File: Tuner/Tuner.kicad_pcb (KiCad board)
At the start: 2 copper layers, 74 parts, among them J1 Barrel_Jack, J2 Input, J3 Conn_01x04_Pin, J4 SWD, J5 output channel, J6 TIM1 output, Q1 NPN, Q2 NPN, Q3 NPN, Q4 NPN, Q5 NPN, SW1 NRST, SW2 SW_SPDT, U1 NE5532, U2 AMS1117-3.3, U3 STM32F411RETx, Y1 16Mhz

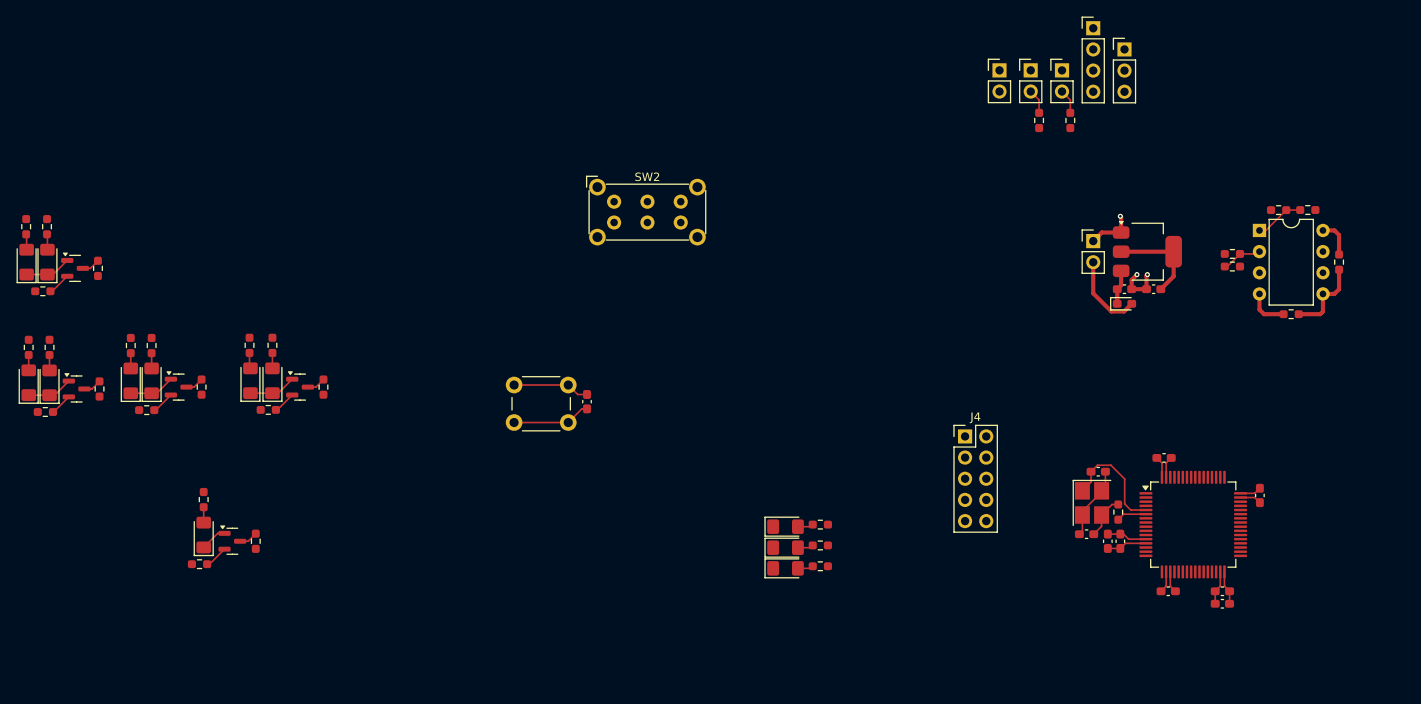
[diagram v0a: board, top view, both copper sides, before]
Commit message: removed the LED drivers and finished first layout placement for the PCB
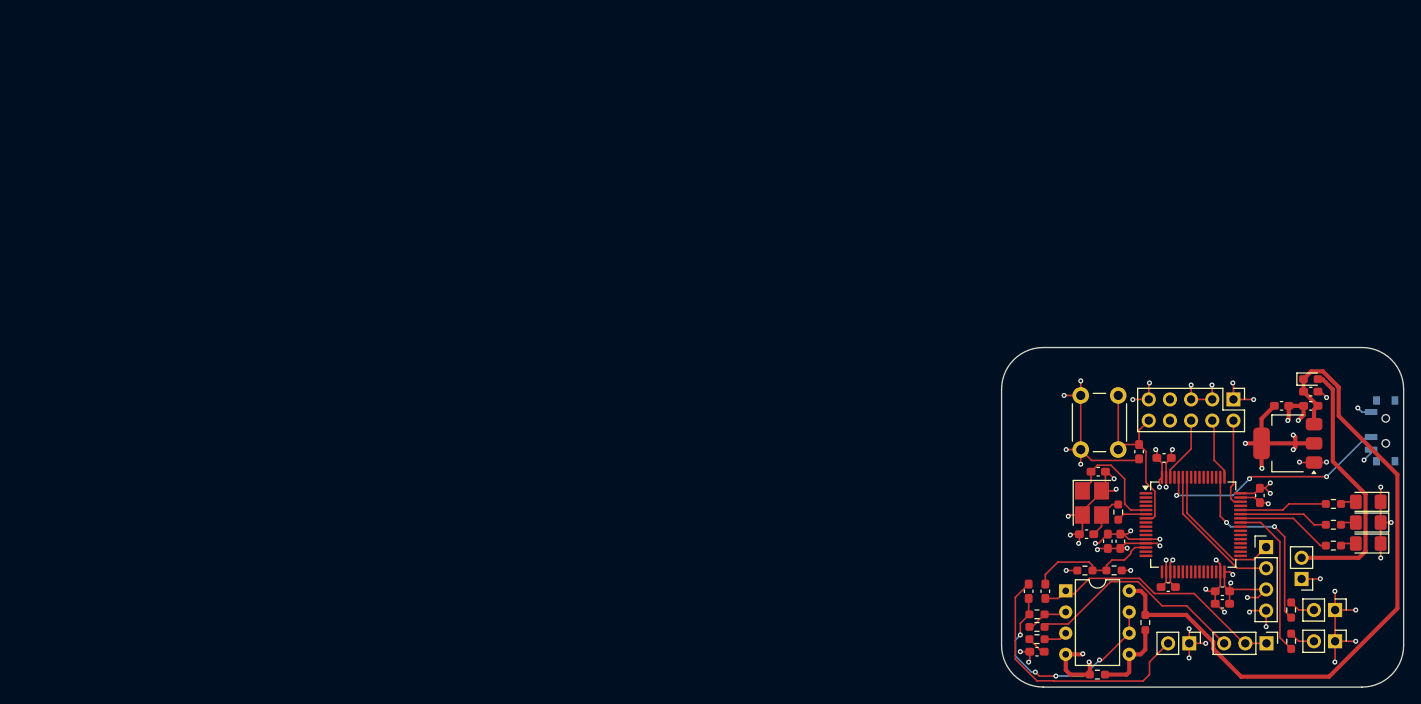
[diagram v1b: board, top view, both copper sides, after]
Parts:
- removed D10, D2, D3, D4, D5, D6, D7, D8, D9: LED, LED_SMD:LED_1206_3216Metric_Pad1.42x1.75mm_HandSolder
- removed Q1, Q2, Q3, Q4, Q5: NPN, Package_TO_SOT_SMD:SOT-23
- removed R10, R11, R12, R13, R14, R15, R16, R9: 470, Resistor_SMD:R_0603_1608Metric_Pad0.98x0.95mm_HandSolder
- removed R17, R18, R19, R20, R21: 6k, Resistor_SMD:R_0603_1608Metric_Pad0.98x0.95mm_HandSolder
- removed R22, R23, R24, R25, R26: 0, Resistor_SMD:R_0603_1608Metric_Pad0.98x0.95mm_HandSolder
- removed the R8 at (23.2, 43.2)
- added C12: 1u, Capacitor_SMD:C_0603_1608Metric_Pad1.08x0.95mm_HandSolder, F.Cu at (143.0, 87.0)
- added C13: 10n, Capacitor_SMD:C_0603_1608Metric_Pad1.08x0.95mm_HandSolder, F.Cu at (142.0, 94.2)
- added C14: 1u, Capacitor_SMD:C_0603_1608Metric_Pad1.08x0.95mm_HandSolder, F.Cu at (141.0, 87.0)
- added C6: 1u, Capacitor_SMD:C_0603_1608Metric_Pad1.08x0.95mm_HandSolder, F.Cu at (174.8, 63.0)
- added r4: 22k, Resistor_SMD:R_0603_1608Metric_Pad0.98x0.95mm_HandSolder, F.Cu at (142.0, 92.8)
- SW2: footprint Button_Switch_THT:SW_E-Switch_EG2219_DPDT_Angled -> Button_Switch_SMD:SW_SPDT_PCM12; moved to B.Cu
- moved SW2 96.3 mm to (183.5, 67.8), turned to -90 degrees
- moved J6 75.9 mm to (177.8, 93.0), turned to -90 degrees
- moved J5 74.4 mm to (177.8, 89.2), turned to -90 degrees
- moved RV1 73.3 mm to (169.5, 93.2), turned to -90 degrees
- moved J2 72.4 mm to (160.3, 93.2), turned to -90 degrees
- moved D13 70.4 mm to (181.8, 76.3), turned to 180 degrees
- moved D12 70.0 mm to (181.8, 78.8), turned to 180 degrees
- moved D11 70.0 mm to (181.8, 81.3), turned to 180 degrees
- moved SW1 68.4 mm to (147.2, 70.0), turned to 90 degrees
- moved R32 67.9 mm to (172.5, 93.0)
- moved C11 66.5 mm to (154.2, 70.2), turned to -90 degrees
- moved R31 66.1 mm to (172.5, 89.2)
- moved J3 65.6 mm to (169.5, 81.7)
- moved R30 62.0 mm to (177.6, 76.5), turned to 0 degrees
- moved R28 61.6 mm to (177.6, 81.5), turned to 0 degrees
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- renumbered C9 to C10, C10 to C11, C11 to C15, C12 to C16, C6 to C7, C7 to C8, C8 to C9, R27 to R28, R28 to R29, R29 to R30, R30 to R31, R31 to R32, R4 to R5, R5 to R6, R6 to R7, R7 to R8
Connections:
- J2 pad 1: Net-(J2-Pin_1) -> GND
- J2 pad 2: GND -> Net-(J2-Pin_2)
- R6 pad 1: GND -> voltage bias
- RV1 pad 1: ADC1_IN0 -> Net-(C12-Pad1)
- RV1 pad 2: ADC1_IN0 -> Net-(C12-Pad1)
- U1 pad 1: ADC1_IN0 -> Net-(C12-Pad1)
- U1 pad 3: Net-(J2-Pin_1) -> Net-(U1A-+)
- U3 pad 38: LED_GREEN -> unconnected-(U3-PC7-Pad38)
- U3 pad 39: LED_YELLOW_1 -> unconnected-(U3-PC8-Pad39)
- U3 pad 40: LED_RED_1 -> unconnected-(U3-PC9-Pad40)
- U3 pad 51: LED_YELLOW_2 -> unconnected-(U3-PC10-Pad51)
- U3 pad 52: LED_RED_2 -> unconnected-(U3-PC11-Pad52)
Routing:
- net GND: track 51.6 -> 138.2 mm, vias 3 -> 47
- net +9V: track 8.64 -> 82.9 mm
- net +3.3V: track 28.1 -> 61.8 mm, vias 0 -> 19
- net Net-(J2-Pin_2): track 0.00 -> 31.9 mm
- net Net-(C12-Pad1): track 0.00 -> 30.9 mm
- net BOOT0: track 0.00 -> 28.5 mm, vias 0 -> 3
- net Net-(R7-Pad2): track 0.00 -> 27.4 mm
- net voltage bias: track 0.00 -> 27.0 mm, vias 0 -> 4
- net TIM2_OC1: track 0.00 -> 23.4 mm, vias 0 -> 2
- net Net-(D1-A): track 9.64 -> 31.3 mm
- net TIM1_CH1: track 0.00 -> 19.1 mm
- net I2C1_SDA: track 0.00 -> 17.1 mm
- net I2C1_SCL: track 0.00 -> 16.7 mm
- net NRST: track 9.43 -> 23.2 mm
- net TIM1_CH2: track 0.00 -> 11.6 mm
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- added copper zone on In2.Cu, net +3.3V
- added copper zone on In1.Cu, net GND
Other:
- board outline added: 48.2 x 40.8 mm
- copper layers 2 -> 4
